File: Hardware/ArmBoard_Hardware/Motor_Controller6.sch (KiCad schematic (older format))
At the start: 13 parts

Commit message: added missing lables to connectors
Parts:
- MC6: symbol MRDT_ICs:VNH5019A_E -> ArmBoard_Hardware-rescue:VNH5019A_E-MRDT_ICs
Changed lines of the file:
@@
 IN_A_6
 $Comp
-L MRDT_ICs:VNH5019A_E U?
+L ArmBoard_Hardware-rescue:VNH5019A_E-MRDT_ICs U?
 U 1 1 62BFB1B6
 P 4925 4600

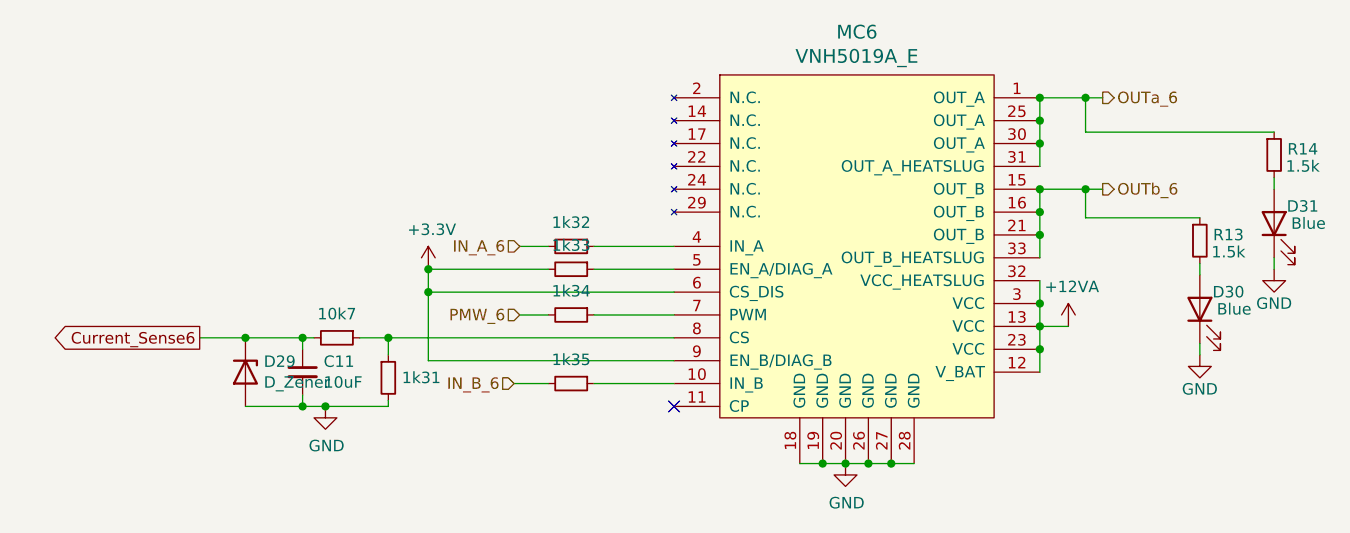
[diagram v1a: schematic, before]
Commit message: schematic changes, encoder changes, led changes
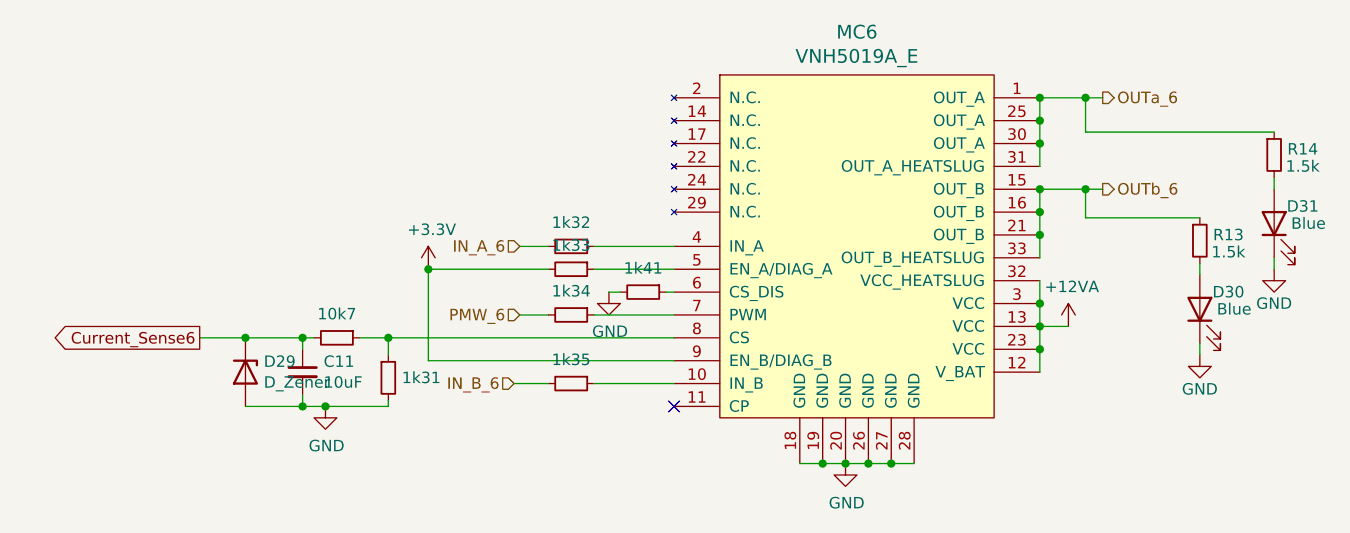
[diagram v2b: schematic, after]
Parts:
- added 1k41: R_Small, Resistor_SMD:R_0603_1608Metric_Pad0.98x0.95mm_HandSolder, symbol Device:R_Small
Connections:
- net +3V3: no longer MC6.6 (CS_DIS)
- net GND: now also 1k41.2
- new net: 1k41.1, MC6.6 (CS_DIS)
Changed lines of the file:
@@
 Wire Wire Line
 	4175 4150 4050 4150
-Wire Wire Line
-	4725 4050 3650 4050
-Wire Wire Line
-	3650 4050 3650 3950
 Connection ~ 3650 3950
 Wire Wire Line
 	4725 4350 3650 4350
-Wire Wire Line
-	3650 4350 3650 4050
-Connection ~ 3650 4050
 Wire Wire Line
 	4725 4250 3475 4250
@@
 Text HLabel 6600 3600 2    50   Output ~ 0
 OUTb_6
+Wire Wire Line
+	3650 3950 3650 4350
+$Comp
+L power:GND #PWR?
+U 1 1 62919207
+P 4440 4050
+AR Path="/63845F20/62919207" Ref="#PWR?"  Part="1"
+AR Path="/628CE14B/62919207" Ref="#PWR?"  Part="1"
+AR Path="/6297969A/62919207" Ref="#PWR?"  Part="1"
+AR Path="/629F46F6/62919207" Ref="#PWR?"  Part="1"
+AR Path="/629F46FD/62919207" Ref="#PWR?"  Part="1"
+AR Path="/62A5CC3B/62919207" Ref="#PWR?"  Part="1"
+AR Path="/62A5CC46/62919207" Ref="#PWR?"  Part="1"
+AR Path="/62AF9C52/62919207" Ref="#PWR?"  Part="1"
+AR Path="/62D2CE1B/62919207" Ref="#PWR?"  Part="1"
+AR Path="/62D4BAA1/62919207" Ref="#PWR010"  Part="1"
+F 0 "#PWR010" H 4440 3800 50  0001 C CNN
+F 1 "GND" H 4445 3877 50  0000 C CNN
+F 2 "" H 4440 4050 50  0001 C CNN
+F 3 "" H 4440 4050 50  0001 C CNN
+	1    4440 4050
+	1    0    0    -1
+$EndComp
+$Comp
+L Device:R_Small 1k?
+U 1 1 6291920D
+P 4590 4050
+AR Path="/63845F20/6291920D" Ref="1k?"  Part="1"
+AR Path="/628CE14B/6291920D" Ref="1k?"  Part="1"
+AR Path="/6297969A/6291920D" Ref="1k?"  Part="1"
+AR Path="/629F46F6/6291920D" Ref="1k?"  Part="1"
+AR Path="/629F46FD/6291920D" Ref="1k?"  Part="1"
+AR Path="/62A5CC3B/6291920D" Ref="1k?"  Part="1"
+AR Path="/62A5CC46/6291920D" Ref="1k?"  Part="1"
+AR Path="/62AF9C52/6291920D" Ref="1k?"  Part="1"
+AR Path="/62C19165/6291920D" Ref="1k?"  Part="1"
+AR Path="/62CA8FD7/6291920D" Ref="1k?"  Part="1"
+AR Path="/62CBA1AC/6291920D" Ref="1k?"  Part="1"
+AR Path="/62CCE879/6291920D" Ref="1k?"  Part="1"
+AR Path="/62CE0B38/6291920D" Ref="1k?"  Part="1"
+AR Path="/62CF1227/6291920D" Ref="1k?"  Part="1"
+AR Path="/62D0C672/6291920D" Ref="1k?"  Part="1"
+AR Path="/62D1BEB1/6291920D" Ref="1k?"  Part="1"
+AR Path="/62D2CE1B/6291920D" Ref="1k?"  Part="1"
+AR Path="/62D3BCB9/6291920D" Ref="1k?"  Part="1"
+AR Path="/62D4BAA1/6291920D" Ref="1k41"  Part="1"
+F 0 "1k41" V 4486 4050 50  0000 C CNN
+F 1 "R_Small" V 4485 4050 50  0001 C CNN
+F 2 "Resistor_SMD:R_0603_1608Metric_Pad0.98x0.95mm_HandSolder" H 4590 4050 50  0001 C CNN
+F 3 "~" H 4590 4050 50  0001 C CNN
+	1    4590 4050
+	0    1    1    0
+$EndComp
+Wire Wire Line
+	4440 4050 4490 4050
+Wire Wire Line
+	4690 4050 4725 4050
 $EndSCHEMATC

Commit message: gerbs added and zipped
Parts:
- MC6: symbol ArmBoard_Hardware-rescue:VNH5019A_E-MRDT_ICs -> MRDT_ICs:VNH5019A_E
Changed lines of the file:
@@
 IN_A_6
 $Comp
-L ArmBoard_Hardware-rescue:VNH5019A_E-MRDT_ICs U?
+L MRDT_ICs:VNH5019A_E U?
 U 1 1 62BFB1B6
 P 4925 4600
